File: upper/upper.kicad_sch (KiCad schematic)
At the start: 1 part, among them U1 RaspberryPi_Pico_W

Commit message: Upper v0.0.1. Pre-routed
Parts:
- added H1, H2, H3, H4: MountingHole, MountingHole:MountingHole_3.2mm_M3_ISO14580, symbol Mechanical:MountingHole
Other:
- note added: "Mounting Holes"

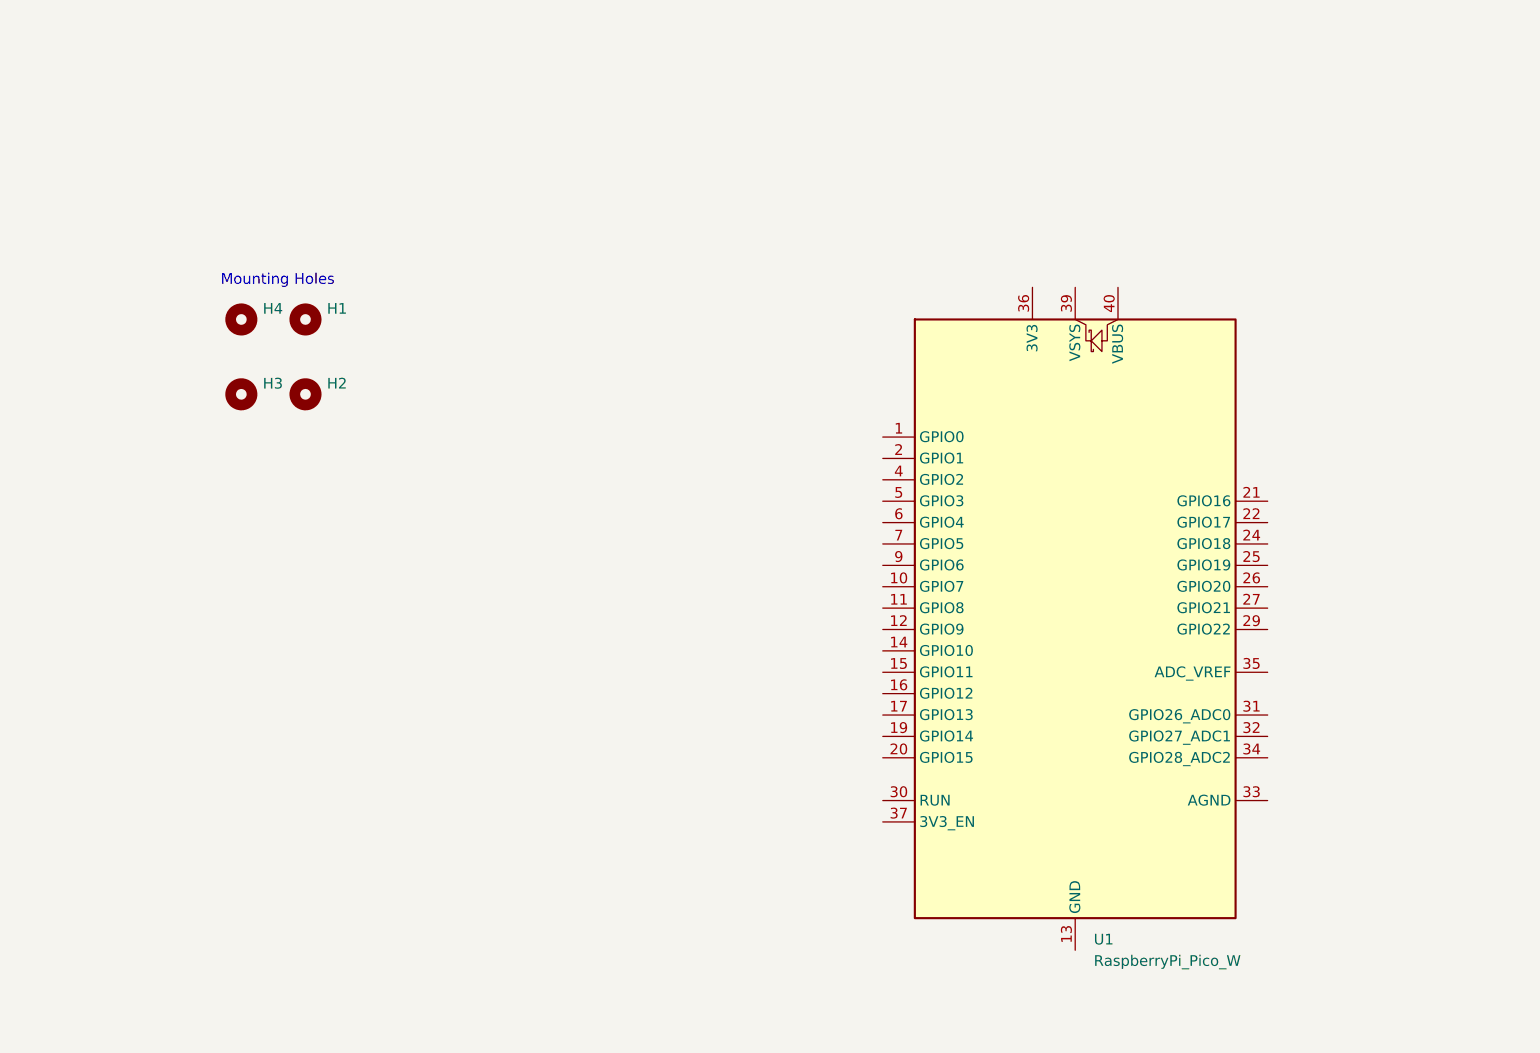
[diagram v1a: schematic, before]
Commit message: Upper v0.1.0. Pre-routed
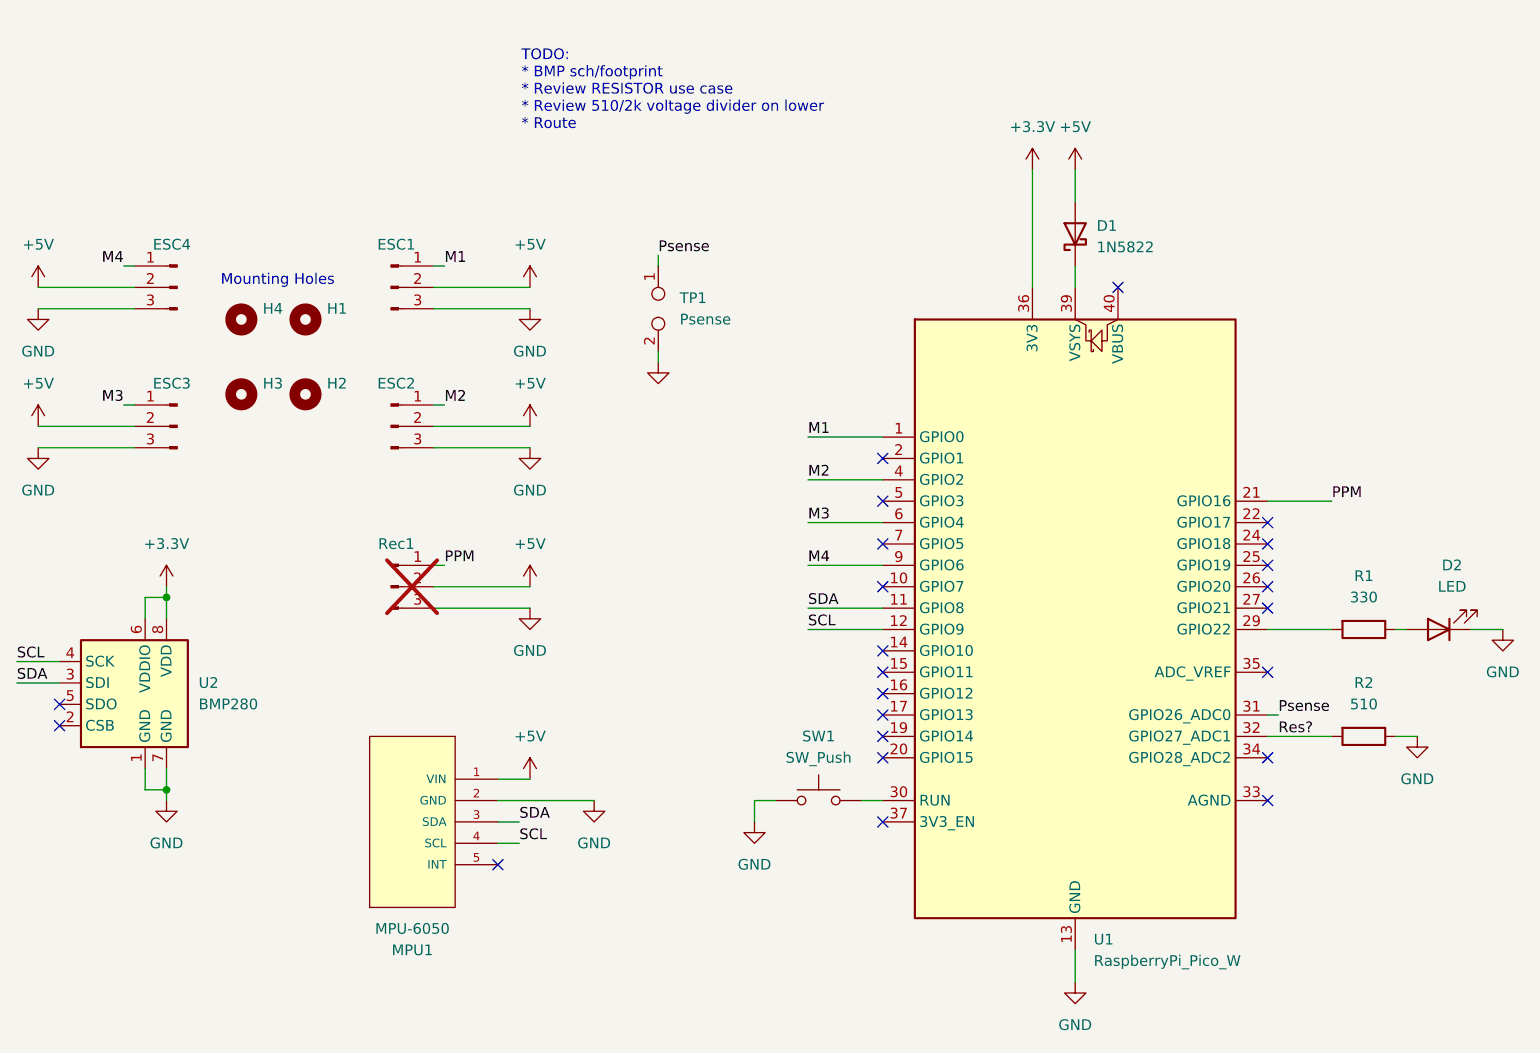
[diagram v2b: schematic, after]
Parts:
- added D1: 1N5822, Diode_SMD:D_SMC_Handsoldering, symbol Device:D_Schottky
- added D2: LED, LED_SMD:LED_1206_3216Metric_Pad1.42x1.75mm_HandSolder, symbol Device:LED
- added ESC1, ESC2, ESC3, ESC4, Rec1: ~, Connector_PinHeader_2.54mm:PinHeader_1x03_P2.54mm_Vertical, symbol Connector:Conn_01x03_Pin
- added MPU1: MPU-6050, SEN0142:SEN0142, symbol SEN0142:SEN0142
- added R1: 330, Resistor_SMD:R_0805_2012Metric_Pad1.20x1.40mm_HandSolder, symbol Device:R
- added R2: 510, Resistor_SMD:R_0201_0603Metric_Pad0.64x0.40mm_HandSolder, symbol Device:R
- added SW1: SW_Push, Button_Switch_SMD:SW_Push_1P1T_NO_6x6mm_H9.5mm, symbol Switch:SW_Push
- added TP1: Psense, TestPoint:TestPoint_2Pads_Pitch2.54mm_Drill0.8mm, symbol Connector:TestPoint_2Pole
- added U2: BMP280, symbol Sensor_Pressure:BMP280
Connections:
- net M1: now reaches U1.1 (GPIO0)
- net M1: now also ESC1.1 (Pin_1)
- net SDA: now reaches U1.11 (GPIO8)
- net SDA: now also MPU1.3 (SDA), U2.3 (SDI)
- net SCL: now reaches U1.12 (GPIO9)
- net SCL: now also MPU1.4 (SCL), U2.4 (SCK)
- net GND: now reaches U1.13 (GND), U1.18 (GND), U1.23 (GND), U1.28 (GND), U1.3 (GND), U1.38 (GND), U1.8 (GND)
- net GND: now also D2.1 (K), ESC1.3 (Pin_3), ESC2.3 (Pin_3), ESC3.3 (Pin_3), ESC4.3 (Pin_3), MPU1.2 (GND), R2.1, Rec1.3 (Pin_3), SW1.1, TP1.2, U2.1 (GND), U2.7 (GND)
- net PPM: now reaches U1.21 (GPIO16)
- net PPM: now also Rec1.1 (Pin_1)
- net at U1.29 (GPIO22): now also R1.2
- net at U1.30 (RUN): now also SW1.2
- net Psense: now reaches U1.31 (GPIO26_ADC0)
- net Psense: now also TP1.1
- net Res?: now reaches U1.32 (GPIO27_ADC1)
- net Res?: now also R2.2
- net +3.3V: now reaches U1.36 (3V3)
- net +3.3V: now also U2.6 (VDDIO), U2.8 (VDD)
- net at U1.39 (VSYS): now also D1.1 (K)
- net M2: now reaches U1.4 (GPIO2)
- net M2: now also ESC2.1 (Pin_1)
- net M3: now reaches U1.6 (GPIO4)
- net M3: now also ESC3.1 (Pin_1)
- net M4: now reaches U1.9 (GPIO6)
- net M4: now also ESC4.1 (Pin_1)
- new net: D2.2 (A), R1.1
- new net +5V: D1.2 (A), ESC1.2 (Pin_2), ESC2.2 (Pin_2), ESC3.2 (Pin_2), ESC4.2 (Pin_2), MPU1.1 (VIN), Rec1.2 (Pin_2)
- no-connect marks 0 -> 23
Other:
- note added: "TODO: * BMP sch/footprint * Review RESISTOR use case * Review 510/2k voltage divider on lower * Route"

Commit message: Upper/Lower: v0.2.0. Pre-routed
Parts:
- removed R2: 510, Resistor_SMD:R_0201_0603Metric_Pad0.64x0.40mm_HandSolder, symbol Device:R
- removed U2: BMP280, symbol Sensor_Pressure:BMP280
- added BMP1: Adafruit-BMP280, upper-all:adafruit-bmp280, symbol upper-all:Adafruit-BMP280
- added JP1, JP3, JP4: Jumper_2_Open, Jumper:SolderJumper-2_P1.3mm_Open_RoundedPad1.0x1.5mm, symbol Jumper:Jumper_2_Open
- added JP2: Jumper_2_Bridged, Jumper:SolderJumper-2_P1.3mm_Bridged_RoundedPad1.0x1.5mm, symbol Jumper:Jumper_2_Bridged
- added TP2: Vsense, TestPoint:TestPoint_2Pads_Pitch2.54mm_Drill0.8mm, symbol Connector:TestPoint_2Pole
- TP1: value Psense -> Isense
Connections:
- net +3.3V: now also BMP1.1 (VIN)
- net +5V: now also JP1.2 (B), JP2.2 (B), JP3.1 (A), JP4.1 (A); no longer ESC1.2 (Pin_2), ESC2.2 (Pin_2), ESC3.2 (Pin_2), ESC4.2 (Pin_2)
- net GND: now also BMP1.3 (GND), TP2.2
- net SCL: now also BMP1.4 (SCK/SCL)
- net SDA: now also BMP1.6 (SDI/SDA)
- net Psense renamed Isense
- net Res? renamed Vsense
- net Vsense: now also TP2.1
- new net: ESC2.2 (Pin_2), JP2.1 (A)
- new net: ESC3.2 (Pin_2), JP3.2 (B)
- new net: ESC4.2 (Pin_2), JP4.2 (B)
- new net: ESC1.2 (Pin_2), JP1.1 (A)
- no-connect marks 23 -> 24
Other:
- note added: "TODO: * Review RESISTOR use case * Review 510/2k voltage divider on lower * Route"
- note removed: "TODO: * BMP sch/footprint * Review RESISTOR use case * Review 510/2k voltage divider on lower * Route"

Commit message: Upper/Lower: v0.2.0. Routed
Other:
- note removed: "TODO: * Review RESISTOR use case * Review 510/2k voltage divider on lower * Route"
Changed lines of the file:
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@@
-		)
-	)
-	(text "TODO:\n* Review RESISTOR use case\n* Review 510/2k voltage divider on lower\n* Route"
-		(exclude_from_sim no)
-		(at 80.264 28.702 0)
-		(effects
-			(font
-				(size 1.27 1.27)
-			)
-			(justify left)
 		)
 	)

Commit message: Upper/Lower: Add post-assembly fixup comments
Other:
- note added: "V1 issues: * R1 is 330 0805 which we don't have. Using 470 * BMP1 mounting hole placement is wrong"
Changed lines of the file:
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@@
+		)
+	)
+	(text "V1 issues:\n* R1 is 330 0805 which we don't have. Using 470\n* BMP1 mounting hole placement is wrong"
+		(exclude_from_sim no)
+		(at 83.7795 26.6053 0)
+		(effects
+			(font
+				(size 1.27 1.27)
+			)
+			(justify left)
 		)
 	)

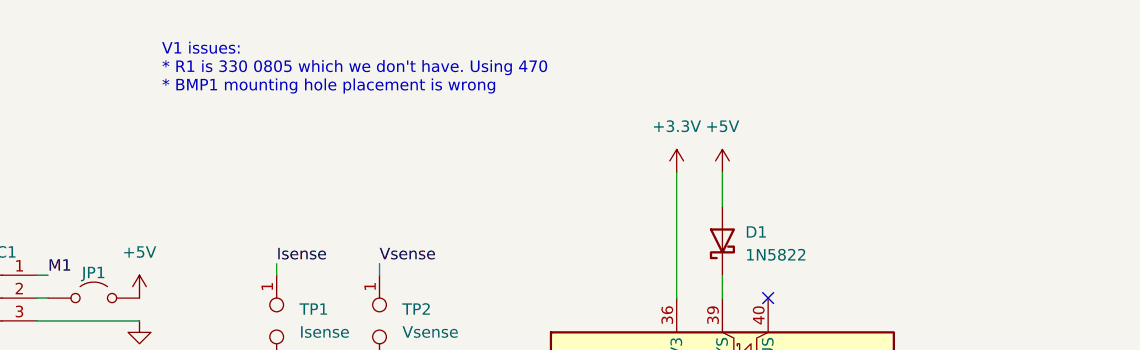
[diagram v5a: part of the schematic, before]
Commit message: Upper/Lower: Add notes
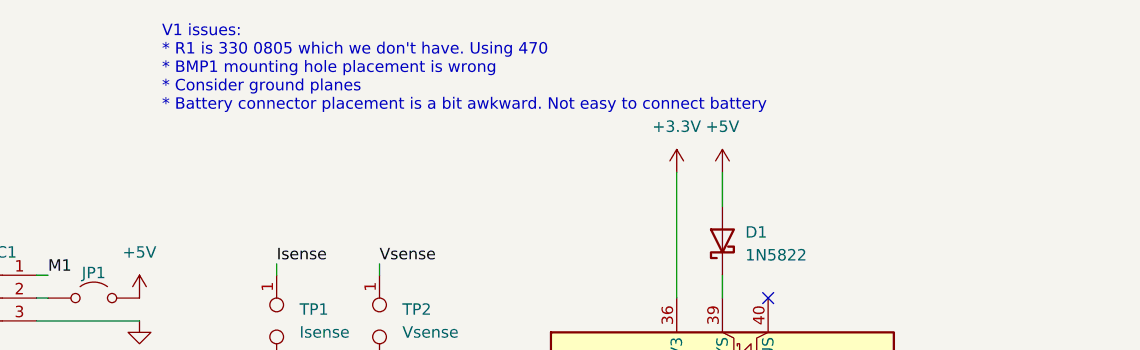
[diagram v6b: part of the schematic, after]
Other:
- note added: "V1 issues: * R1 is 330 0805 which we don't have. Using 470 * BMP1 mounting hole placement is wrong * Consider ground planes * Battery connector placement is a bit awkward. Not easy to connect battery"
- note removed: "V1 issues: * R1 is 330 0805 which we don't have. Using 470 * BMP1 mounting hole placement is wrong"
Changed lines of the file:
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@@
 		)
 	)
-	(text "V1 issues:\n* R1 is 330 0805 which we don't have. Using 470\n* BMP1 mounting hole placement is wrong"
+	(text "V1 issues:\n* R1 is 330 0805 which we don't have. Using 470\n* BMP1 mounting hole placement is wrong\n* Consider ground planes\n* Battery connector placement is a bit awkward. Not easy to connect battery"
 		(exclude_from_sim no)
 		(at 83.7795 26.6053 0)

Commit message: Upper: Add to v1 issues list
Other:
- note added: "V1 issues: * R1 is 330 0805 which we don't have. Using 470 * BMP1 mounting hole placement is wrong * Consider ground planes * Battery connector placement is a bit awkward. Not easy to connect battery * Add +/-ve roll/pitch/yaw to silkscreen"
- note removed: "V1 issues: * R1 is 330 0805 which we don't have. Using 470 * BMP1 mounting hole placement is wrong * Consider ground planes * Battery connector placement is a bit awkward. Not easy to connect battery"
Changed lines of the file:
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@@
 		)
 	)
-	(text "V1 issues:\n* R1 is 330 0805 which we don't have. Using 470\n* BMP1 mounting hole placement is wrong\n* Consider ground planes\n* Battery connector placement is a bit awkward. Not easy to connect battery"
+	(text "V1 issues:\n* R1 is 330 0805 which we don't have. Using 470\n* BMP1 mounting hole placement is wrong\n* Consider ground planes\n* Battery connector placement is a bit awkward. Not easy to connect battery\n* Add +/-ve roll/pitch/yaw to silkscreen"
 		(exclude_from_sim no)
 		(at 83.7795 26.6053 0)
